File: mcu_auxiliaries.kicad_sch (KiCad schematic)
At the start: 30 parts, among them Y1 12MHz 18pF, Y2 12MHz 18pF

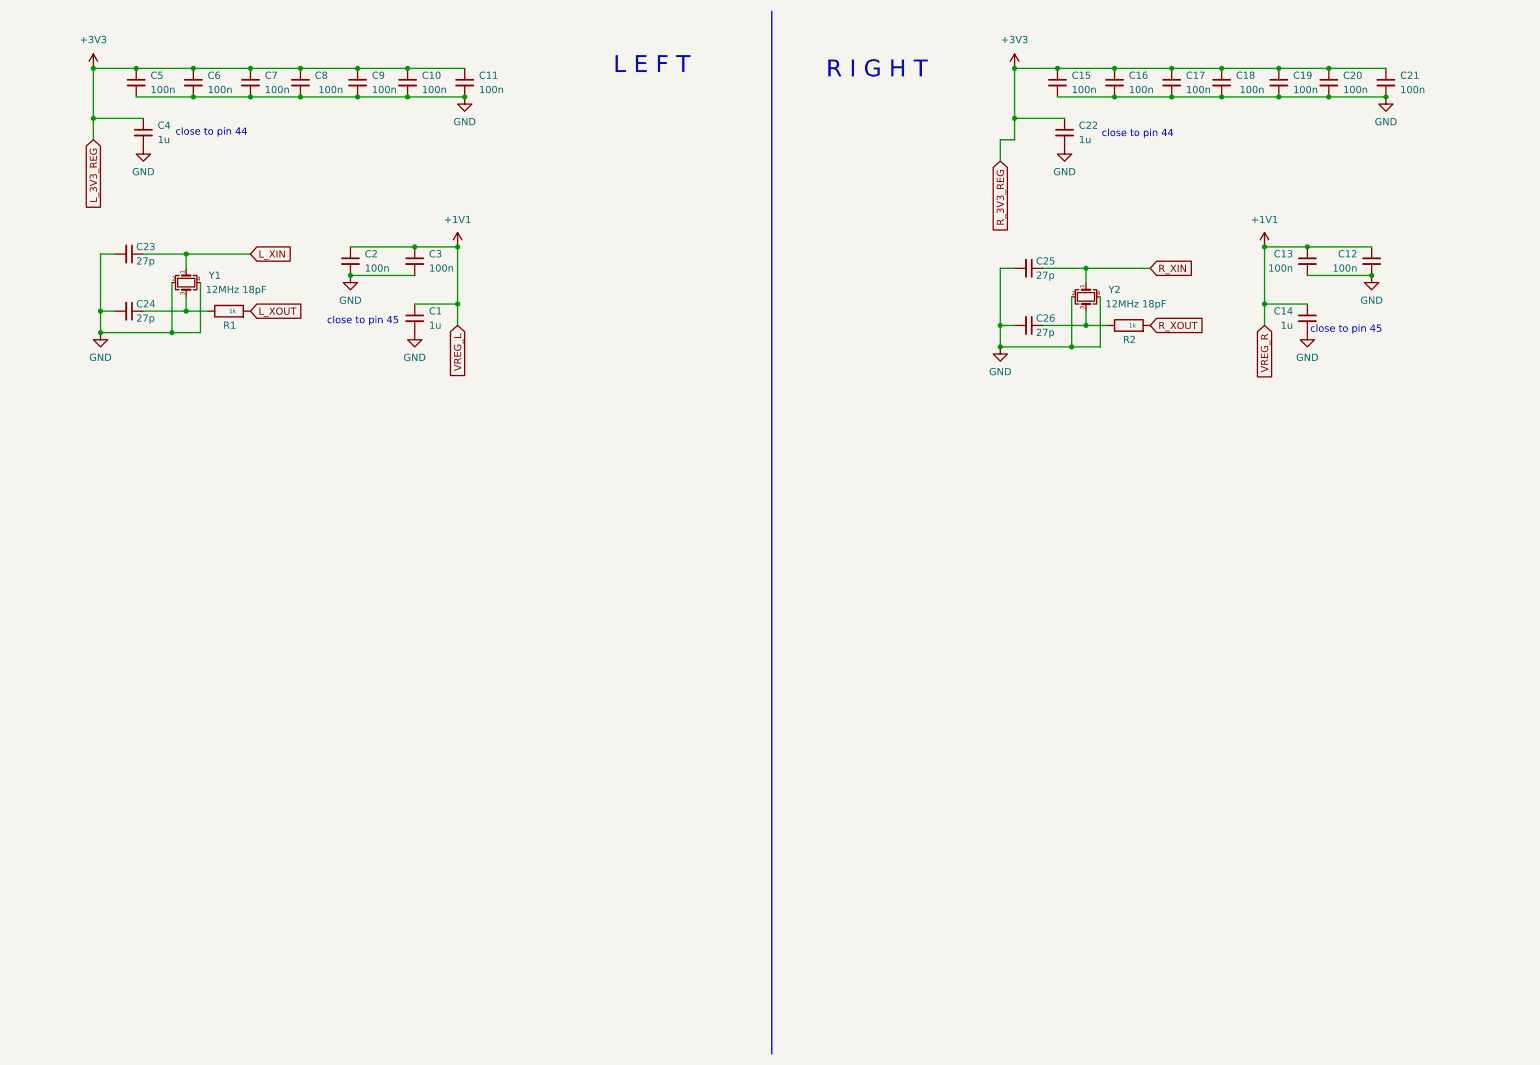
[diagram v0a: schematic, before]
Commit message: Add qspi flash
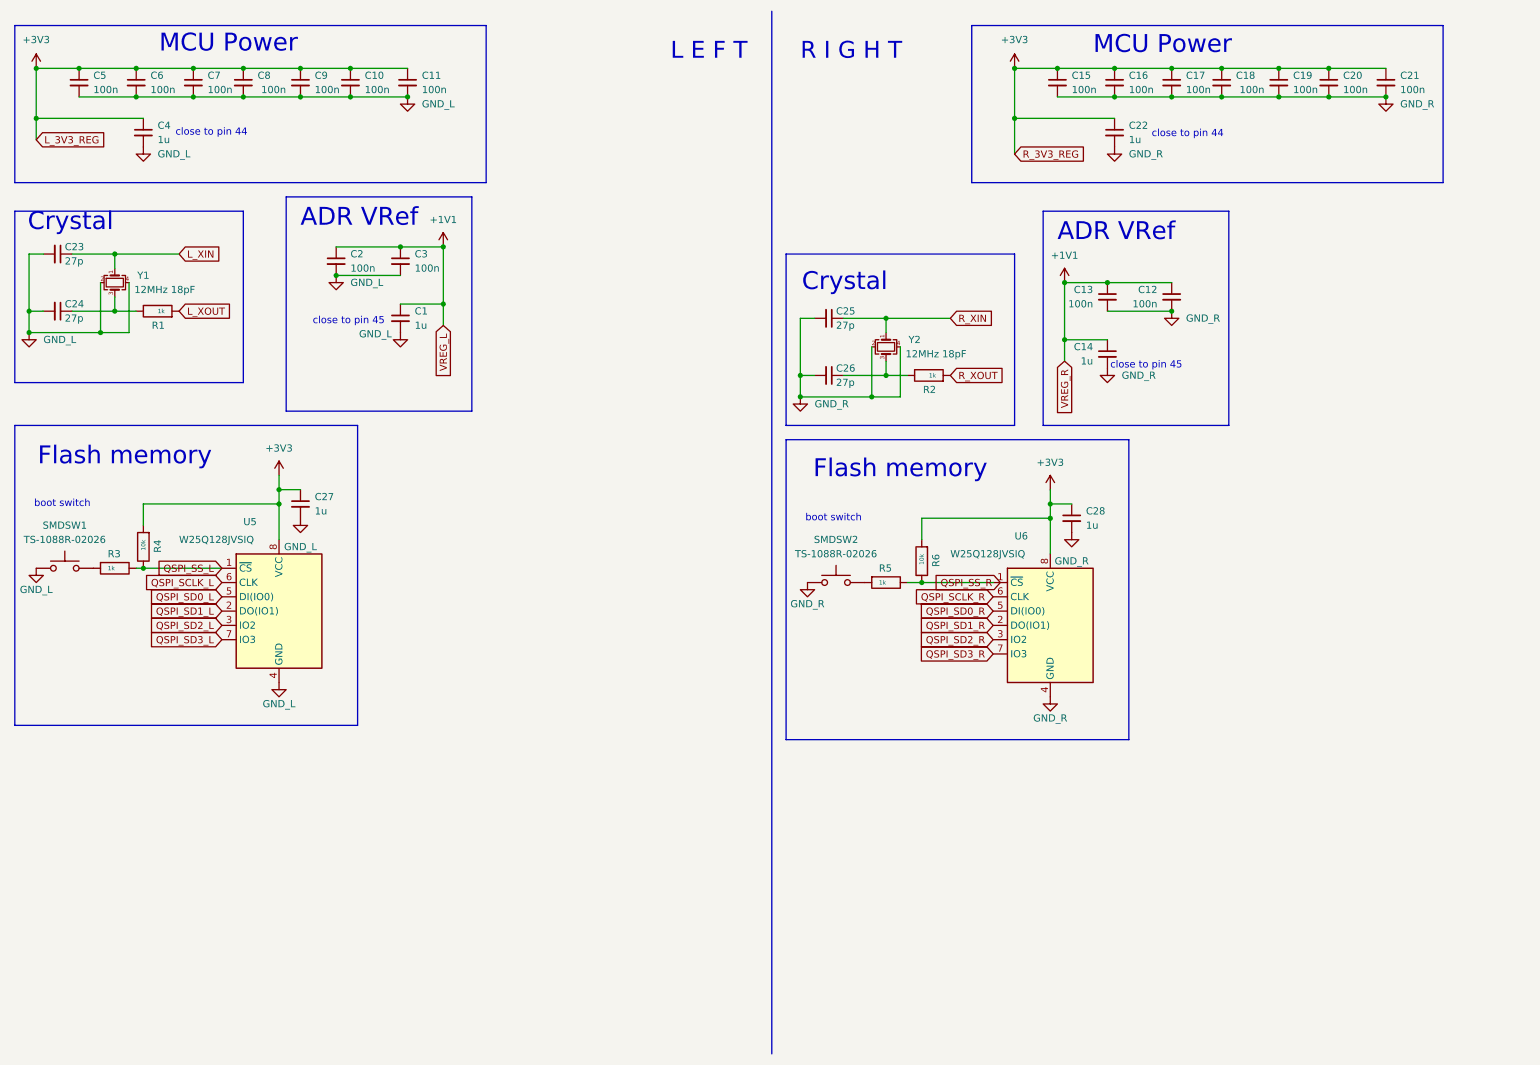
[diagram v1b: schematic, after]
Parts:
- added C27, C28: 1u, Capacitor_SMD:C_0402_1005Metric, symbol Device:C_Small
- added R3, R5: 1k, Resistor_SMD:R_0402_1005Metric, symbol Device:R
- added R4, R6: 10k, Resistor_SMD:R_0402_1005Metric, symbol Device:R
- added SMDSW1, SMDSW2: TS-1088R-02026, kbd_local:TS-1088R-02026, symbol Switch:SW_Push
- added U5, U6: W25Q128JVSIQ, Package_SO:SOIC-8_5.23x5.23mm_P1.27mm, symbol Memory_Flash:W25Q128JVS
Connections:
- net +3V3: now also C27.1, C28.1, R4.2, R6.2, U5.8 (VCC), U6.8 (VCC)
- net GND renamed GND_L
- net GND_L: now also C27.2, SMDSW1.1, U5.4 (GND); no longer C12.2, C13.2, C14.2, C15.2, C16.2, C17.2, C18.2, C19.2, C20.2, C21.2, C22.2, C25.2, C26.2, Y2.2, Y2.4
- new net: R5.2, SMDSW2.2
- new net: R5.1, R6.1, U6.1 (~{CS})
- new net: R3.2, SMDSW1.2
- new net GND_R: C12.2, C13.2, C14.2, C15.2, C16.2, C17.2, C18.2, C19.2, C20.2, C21.2, C22.2, C25.2, C26.2, C28.2, SMDSW2.1, U6.4 (GND), Y2.2, Y2.4
- new net QSPI_SCLK_L: U5.6 (CLK)
- new net QSPI_SCLK_R: U6.6 (CLK)
- new net QSPI_SD0_L: U5.5 (DI(IO0))
- new net QSPI_SD0_R: U6.5 (DI(IO0))
- new net QSPI_SD1_L: U5.2 (DO(IO1))
- new net QSPI_SD1_R: U6.2 (DO(IO1))
- new net QSPI_SD2_L: U5.3 (IO2)
- new net QSPI_SD2_R: U6.3 (IO2)
- new net QSPI_SD3_L: U5.7 (IO3)
- new net QSPI_SD3_R: U6.7 (IO3)
- new net QSPI_SS_L: R3.1, R4.1, U5.1 (~{CS})
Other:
- note added: "ADR VRef"
- note added: "Crystal"
- note added: "Flash memory"
- note added: "MCU Power"
- note added: "boot switch"
- moved on the sheet: C1, C10, C11, C12, C13, C14, C2, C22, C23, C24, C25, C26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

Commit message: Added usb-c port for split access
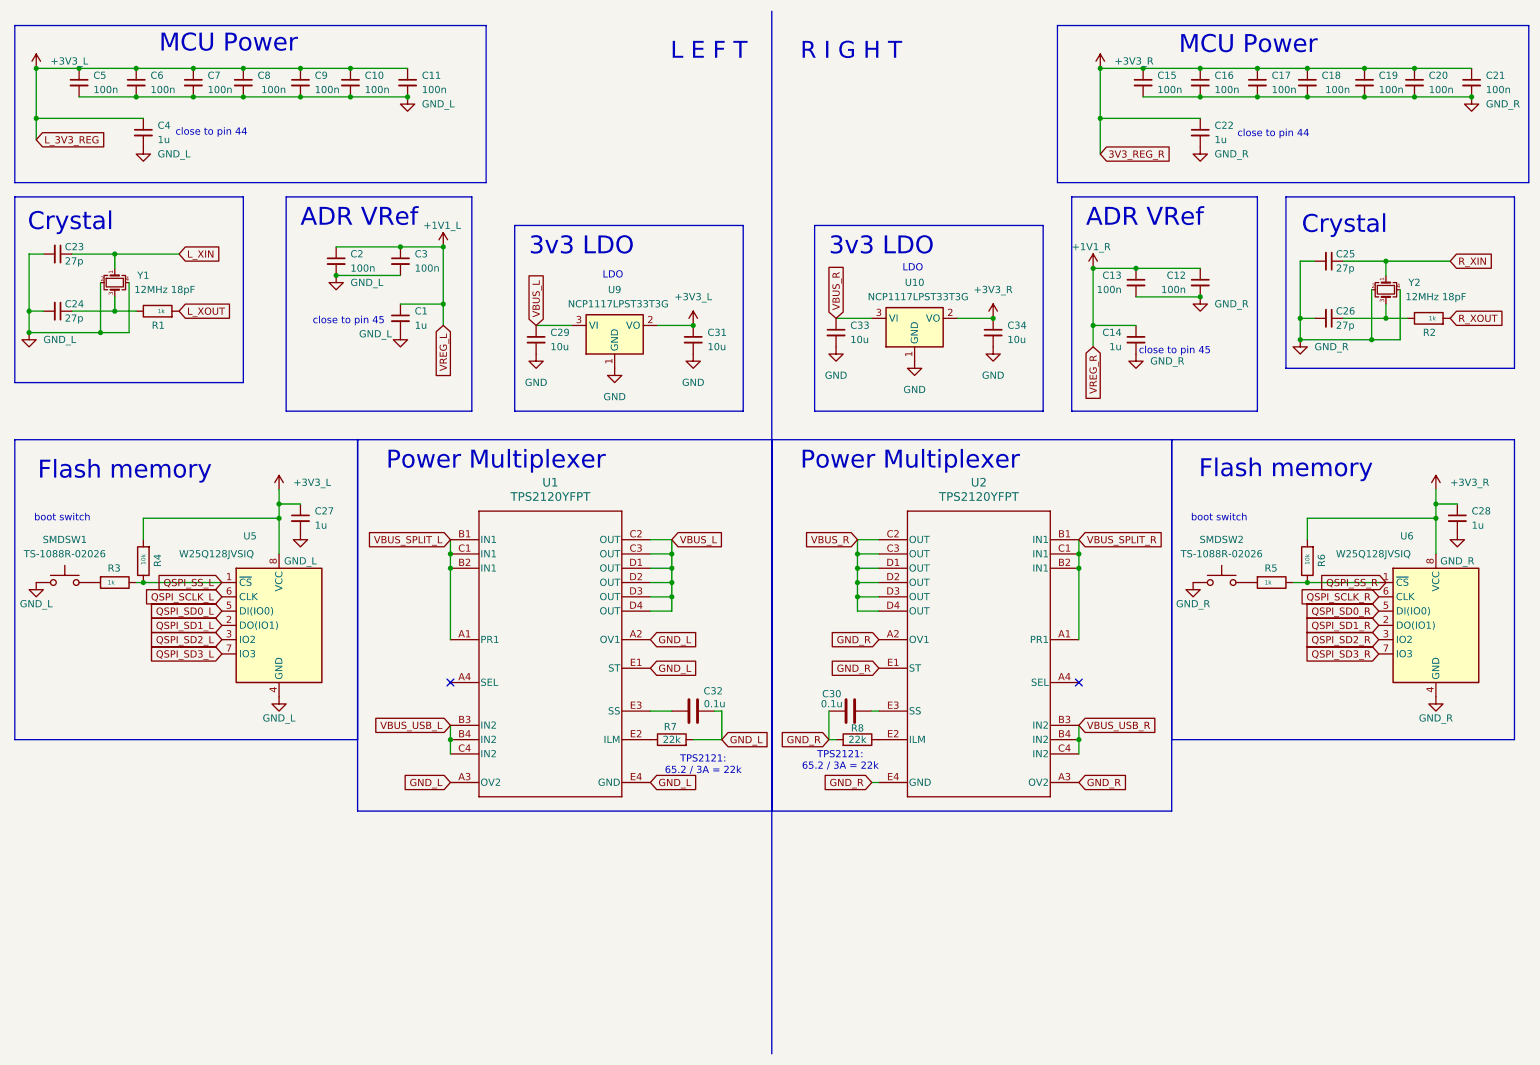
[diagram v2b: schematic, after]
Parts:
- added C29, C31, C33, C34: 10u, Capacitor_SMD:C_0402_1005Metric, symbol Device:C_Small
- added C30, C32: 0.1u, symbol Device:C
- added R7, R8: 22k, symbol Device:R
- added U1, U2: TPS2120YFPT, YFP0020AAAA, symbol TPS2120YFPT:TPS2120YFPT
- added U10, U9: NCP1117LPST33T3G, Package_TO_SOT_SMD:SOT-223-3_TabPin2, symbol Regulator_Linear:NCP1117-3.3_SOT223
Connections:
- net GND_L: now also C32.2, R7.2, U1.A2 (OV1), U1.A3 (OV2), U1.E1 (ST), U1.E4 (GND)
- net GND_R: now also C30.2, R8.2, U2.A2 (OV1), U2.A3 (OV2), U2.E1 (ST), U2.E4 (GND)
- net +1V1 renamed +1V1_L
- net +1V1_L: no longer C12.1, C13.1, C14.1
- net +3V3 renamed +3V3_L
- net +3V3_L: now also C31.1, U9.2 (VO); no longer C15.1, C16.1, C17.1, C18.1, C19.1, C20.1, C21.1, C22.1, C28.1, R6.2, U6.8 (VCC)
- new net: C32.1, U1.E3 (SS)
- new net: R7.1, U1.E2 (ILM)
- new net: R8.1, U2.E2 (ILM)
- new net: C30.1, U2.E3 (SS)
- new net +1V1_R: C12.1, C13.1, C14.1
- new net +3V3_R: C15.1, C16.1, C17.1, C18.1, C19.1, C20.1, C21.1, C22.1, C28.1, C34.1, R6.2, U10.2 (VO), U6.8 (VCC)
- new net GND: C29.2, C31.2, C33.2, C34.2, U10.1 (GND), U9.1 (GND)
- new net VBUS_L: C29.1, U1.C2 (OUT), U1.C3 (OUT), U1.D1 (OUT), U1.D2 (OUT), U1.D3 (OUT), U1.D4 (OUT), U9.3 (VI)
- new net VBUS_R: C33.1, U10.3 (VI), U2.C2 (OUT), U2.C3 (OUT), U2.D1 (OUT), U2.D2 (OUT), U2.D3 (OUT), U2.D4 (OUT)
- new net VBUS_SPLIT_L: U1.A1 (PR1), U1.B1 (IN1), U1.B2 (IN1), U1.C1 (IN1)
- new net VBUS_SPLIT_R: U2.A1 (PR1), U2.B1 (IN1), U2.B2 (IN1), U2.C1 (IN1)
- new net VBUS_USB_L: U1.B3 (IN2), U1.B4 (IN2), U1.C4 (IN2)
- new net VBUS_USB_R: U2.B3 (IN2), U2.B4 (IN2), U2.C4 (IN2)
- no-connect marks 0 -> 2
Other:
- note added: "3v3 LDO"
- note added: "LDO"
- note added: "Power Multiplexer"
- note added: "TPS2121: 65.2 / 3A = 22k"
- moved on the sheet: C12, C13, C14, C15, C16, C17, C18, C19, C20, C21, C22, C25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

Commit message: Initial routing an placement
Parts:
- removed C30: 0.1u, symbol Device:C
- removed R8: 22k, symbol Device:R
- removed SMDSW1, SMDSW2: TS-1088R-02026, kbd_local:TS-1088R-02026, symbol Switch:SW_Push
- removed U1, U2: TPS2120YFPT, YFP0020AAAA, symbol TPS2120YFPT:TPS2120YFPT
- added C35: 0.1u, Capacitor_SMD:C_0402_1005Metric, symbol Device:C
- added R10: 22k, Resistor_SMD:R_0402_1005Metric, symbol Device:R
- added U1, U2: TPS2121RUXR, TOTEMlib:TPS2121, symbol TOTEM:TPS2121RUXR
- C32: footprint (none) -> Capacitor_SMD:C_0402_1005Metric
- R7: footprint (none) -> Resistor_SMD:R_0402_1005Metric
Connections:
- net GND_L: now also C29.2, C31.2, U9.1 (GND), U1.12 (GND), U1.4 (OV2), U1.5 (OV1), U1.9 (ST)
- net GND_R: now also C33.2, C34.2, U10.1 (GND), C35.2, R10.2, U2.12 (GND), U2.4 (OV2), U2.5 (OV1), U2.9 (ST)
- net QSPI_SS_R: now also R5.1, R6.1, U6.1 (~{CS})
- net VBUS_L: now also U1.1 (OUT), U1.8 (OUT)
- net VBUS_R: now also U2.1 (OUT), U2.8 (OUT)
- net VBUS_SPLIT_L: now also U1.6 (PR1), U1.7 (IN1)
- net VBUS_SPLIT_R: now also U2.6 (PR1), U2.7 (IN1)
- net VBUS_USB_L: now also U1.2 (IN2)
- net VBUS_USB_R: now also U2.2 (IN2)
- net at C32.1: now also U1.11 (SS)
- net RESET_R: now reaches R5.2
- net at R7.1: now also U1.10 (ILM)
- net RESET_L: now reaches R3.2
- removed net GND: C29.2, C31.2, C33.2, C34.2, U10.1 (GND), U9.1 (GND)
- net L_XIN renamed XIN_L
- net L_XOUT renamed XOUT_L
- net R_XIN renamed XIN_R
- net R_XOUT renamed XOUT_R
- new net: R10.1, U2.10 (ILM)
- new net: C35.1, U2.11 (SS)
- no-connect marks 2 -> 0
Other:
- moved on the sheet: C32, R7
